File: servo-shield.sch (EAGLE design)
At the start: 23 parts, among them IC1 24AA01P, K1 PIN20X2

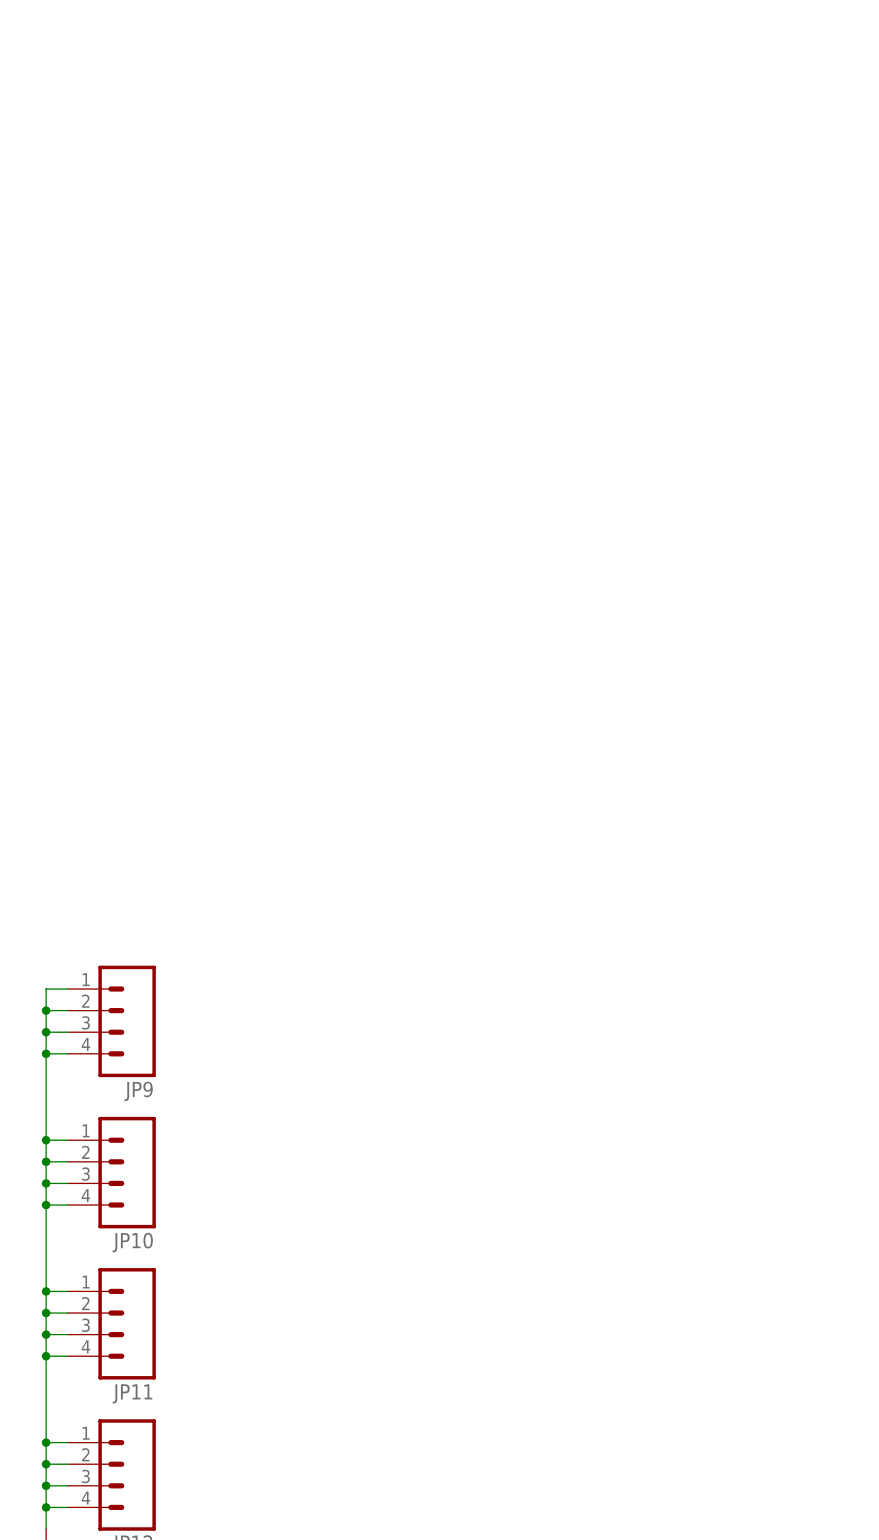
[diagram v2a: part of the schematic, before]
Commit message: Added power connector + regulator
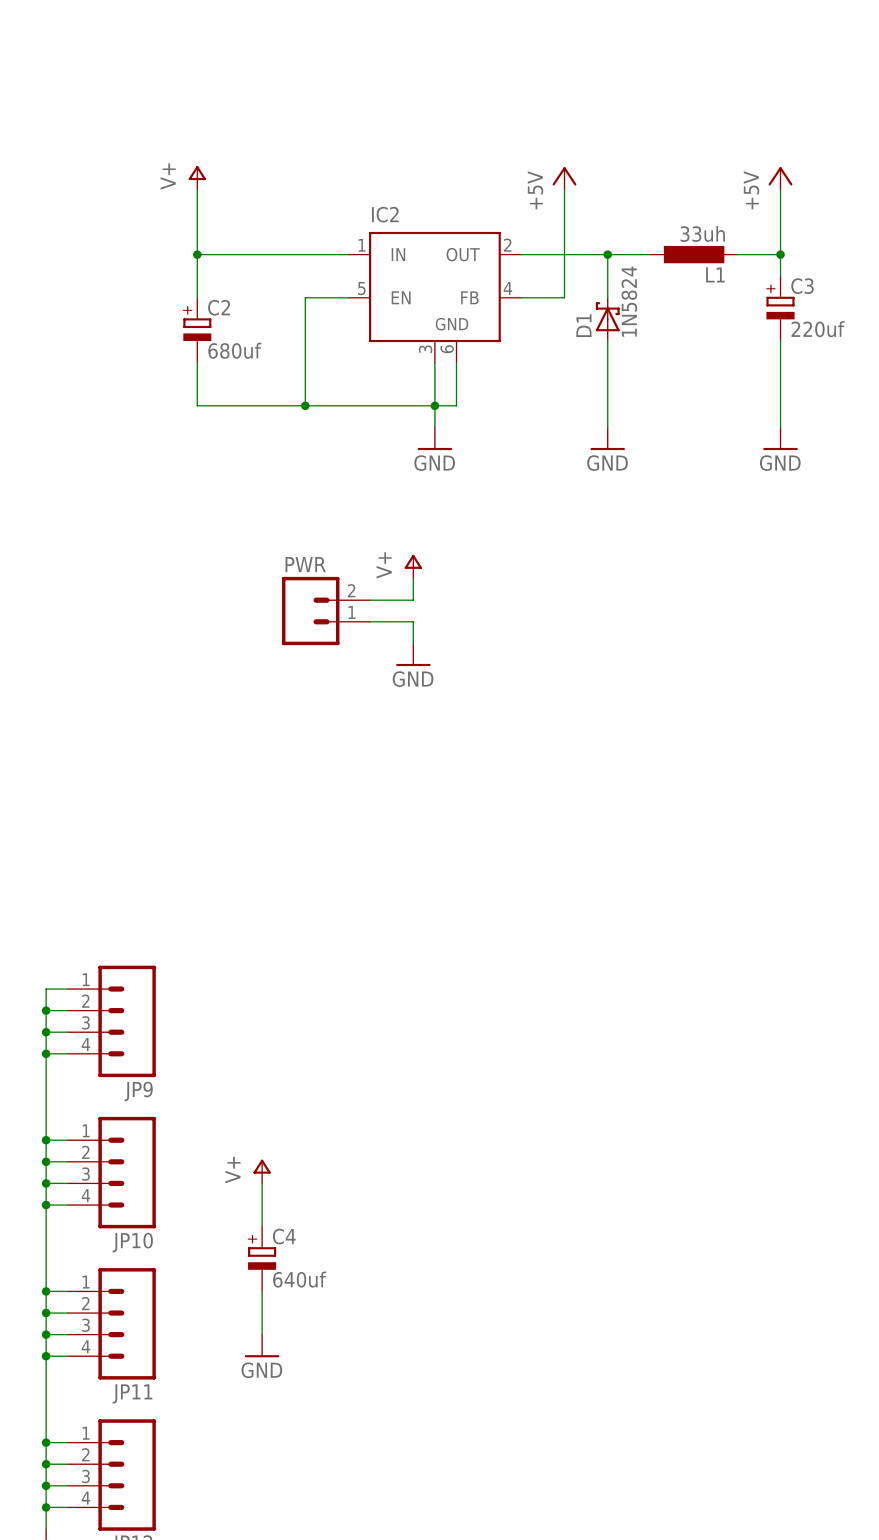
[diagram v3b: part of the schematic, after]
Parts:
- added C2: 680uf, rcl:CPOL-EUE2.5-6
- added C3: 220uf, rcl:CPOL-EUE2.5-6
- added C4: 640uf, rcl:CPOL-EUE2.5-6
- added D1: 1N5824, diode:1N5817-B
- added IC2: (no value), linear:LM2596S
- added L1: 33uh, rcl:L-EU0207/10
- added PWR: M02JST-PTH-2, SparkFun-Connectors:M02JST-PTH-2
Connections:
- new net N$40: D1.C, IC2.OUT, L1.1
- net +5V: now also C3.+, IC2.FB, L1.2
- net GND: now also C2.-, C3.-, C4.-, D1.A, IC2.EN, IC2.GND, IC2.GND@1, PWR.1
- net V+: now also C2.+, C4.+, IC2.IN, PWR.2
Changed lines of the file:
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@@
 <part name="JP11" library="SparkFun-Connectors" deviceset="M04" device="LOCK"/>
 <part name="JP12" library="SparkFun-Connectors" deviceset="M04" device="LOCK"/>
+<part name="P+2" library="supply1" deviceset="+5V" device=""/>
+<part name="P+4" library="supply1" deviceset="V+" device=""/>
+<part name="GND1" library="supply1" deviceset="GND" device=""/>
+<part name="GND6" library="supply1" deviceset="GND" device=""/>
+<part name="GND8" library="supply1" deviceset="GND" device=""/>
+<part name="GND9" library="supply1" deviceset="GND" device=""/>
+<part name="IC2" library="linear" deviceset="LM2596S" device=""/>
+<part name="C2" library="rcl" deviceset="CPOL-EU" device="E2.5-6" value="680uf"/>
+<part name="L1" library="rcl" deviceset="L-EU" device="0207/10" value="33uh"/>
+<part name="D1" library="diode" deviceset="1N581*" device="" technology="7-B" value="1N5824"/>
+<part name="P+5" library="supply1" deviceset="+5V" device=""/>
+<part name="C3" library="rcl" deviceset="CPOL-EU" device="E2.5-6" value="220uf"/>
+<part name="C4" library="rcl" deviceset="CPOL-EU" device="E2.5-6" value="640uf"/>
+<part name="P+6" library="supply1" deviceset="V+" device=""/>
+<part name="PWR" library="SparkFun-Connectors" deviceset="M02" device="JST-PTH-2" value=""/>
+<part name="P+7" library="supply1" deviceset="V+" device=""/>
+<part name="GND11" library="supply1" deviceset="GND" device=""/>
 </parts>
 <sheets>
@@
 <instance part="JP11" gate="G$1" x="208.28" y="50.8" rot="R180"/>
 <instance part="JP12" gate="G$1" x="208.28" y="33.02" rot="R180"/>
+<instance part="P+2" gate="1" x="287.02" y="185.42"/>
+<instance part="P+4" gate="1" x="218.44" y="185.42"/>
+<instance part="GND1" gate="1" x="246.38" y="152.4"/>
+<instance part="GND6" gate="1" x="266.7" y="152.4"/>
+<instance part="GND8" gate="1" x="287.02" y="152.4"/>
+<instance part="GND9" gate="1" x="226.06" y="45.72"/>
+<instance part="IC2" gate="G$1" x="246.38" y="172.72"/>
+<instance part="C2" gate="G$1" x="218.44" y="167.64"/>
+<instance part="L1" gate="G$1" x="276.86" y="175.26" rot="R90"/>
+<instance part="D1" gate="G$1" x="266.7" y="167.64" rot="R90"/>
+<instance part="P+5" gate="1" x="261.62" y="185.42"/>
+<instance part="C3" gate="G$1" x="287.02" y="170.18"/>
+<instance part="C4" gate="G$1" x="226.06" y="58.42"/>
+<instance part="P+6" gate="1" x="226.06" y="68.58"/>
+<instance part="PWR" gate="G$1" x="231.14" y="132.08"/>
+<instance part="P+7" gate="1" x="243.84" y="139.7"/>
+<instance part="GND11" gate="1" x="243.84" y="127"/>
 </instances>
 <busses>
@@
 <pinref part="JP12" gate="G$1" pin="4"/>
 </segment>
+<segment>
+<pinref part="IC2" gate="G$1" pin="EN"/>
+<wire x1="236.22" y1="170.18" x2="231.14" y2="170.18" width="0.1524" layer="91"/>
+<wire x1="231.14" y1="170.18" x2="231.14" y2="157.48" width="0.1524" layer="91"/>
+<pinref part="IC2" gate="G$1" pin="GND"/>
+<wire x1="231.14" y1="157.48" x2="246.38" y2="157.48" width="0.1524" layer="91"/>
+<wire x1="246.38" y1="162.56" x2="246.38" y2="157.48" width="0.1524" layer="91"/>
+<pinref part="GND1" gate="1" pin="GND"/>
+<wire x1="246.38" y1="154.94" x2="246.38" y2="157.48" width="0.1524" layer="91"/>
+<wire x1="246.38" y1="157.48" x2="248.92" y2="157.48" width="0.1524" layer="91"/>
+<pinref part="IC2" gate="G$1" pin="GND@1"/>
+<wire x1="248.92" y1="157.48" x2="248.92" y2="162.56" width="0.1524" layer="91"/>
+<junction x="246.38" y="157.48"/>
+<pinref part="C2" gate="G$1" pin="-"/>
+<wire x1="218.44" y1="162.56" x2="218.44" y2="157.48" width="0.1524" layer="91"/>
+<wire x1="218.44" y1="157.48" x2="231.14" y2="157.48" width="0.1524" layer="91"/>
+<junction x="231.14" y="157.48"/>
+</segment>
+<segment>
+<pinref part="GND6" gate="1" pin="GND"/>
+<pinref part="D1" gate="G$1" pin="A"/>
+<wire x1="266.7" y1="154.94" x2="266.7" y2="165.1" width="0.1524" layer="91"/>
+</segment>
+<segment>
+<pinref part="GND8" gate="1" pin="GND"/>
+<pinref part="C3" gate="G$1" pin="-"/>
+<wire x1="287.02" y1="154.94" x2="287.02" y2="165.1" width="0.1524" layer="91"/>
+</segment>
+<segment>
+<pinref part="C4" gate="G$1" pin="-"/>
+<pinref part="GND9" gate="1" pin="GND"/>
+<wire x1="226.06" y1="53.34" x2="226.06" y2="48.26" width="0.1524" layer="91"/>
+</segment>
+<segment>
+<pinref part="PWR" gate="G$1" pin="1"/>
+<wire x1="238.76" y1="132.08" x2="243.84" y2="132.08" width="0.1524" layer="91"/>
+<pinref part="GND11" gate="1" pin="GND"/>
+<wire x1="243.84" y1="132.08" x2="243.84" y2="129.54" width="0.1524" layer="91"/>
+</segment>
 </net>
 <net name="+3V3" class="0">
@@
 <wire x1="60.96" y1="172.72" x2="60.96" y2="175.26" width="0.1524" layer="91"/>
 <junction x="60.96" y="175.26"/>
+</segment>
+<segment>
+<pinref part="P+2" gate="1" pin="+5V"/>
+<wire x1="287.02" y1="175.26" x2="287.02" y2="182.88" width="0.1524" layer="91"/>
+<pinref part="L1" gate="G$1" pin="2"/>
+<wire x1="281.94" y1="175.26" x2="287.02" y2="175.26" width="0.1524" layer="91"/>
+<pinref part="C3" gate="G$1" pin="+"/>
+<wire x1="287.02" y1="172.72" x2="287.02" y2="175.26" width="0.1524" layer="91"/>
+<junction x="287.02" y="175.26"/>
+</segment>
+<segment>
+<pinref part="IC2" gate="G$1" pin="FB"/>
+<pinref part="P+5" gate="1" pin="+5V"/>
+<wire x1="256.54" y1="170.18" x2="261.62" y2="170.18" width="0.1524" layer="91"/>
+<wire x1="261.62" y1="170.18" x2="261.62" y2="182.88" width="0.1524" layer="91"/>
 </segment>
 </net>
@@
 <junction x="180.34" y="45.72"/>
 </segment>
-</net>
+<segment>
+<pinref part="P+4" gate="1" pin="V+"/>
+<wire x1="218.44" y1="182.88" x2="218.44" y2="175.26" width="0.1524" layer="91"/>
+<pinref part="IC2" gate="G$1" pin="IN"/>
+<wire x1="218.44" y1="175.26" x2="236.22" y2="175.26" width="0.1524" layer="91"/>
+<pinref part="C2" gate="G$1" pin="+"/>
+<wire x1="218.44" y1="170.18" x2="218.44" y2="175.26" width="0.1524" layer="91"/>
+<junction x="218.44" y="175.26"/>
+</segment>
+<segment>
+<pinref part="C4" gate="G$1" pin="+"/>
+<pinref part="P+6" gate="1" pin="V+"/>
+<wire x1="226.06" y1="60.96" x2="226.06" y2="66.04" width="0.1524" layer="91"/>
+</segment>
+<segment>
+<pinref part="PWR" gate="G$1" pin="2"/>
+<wire x1="238.76" y1="134.62" x2="243.84" y2="134.62" width="0.1524" layer="91"/>
+<pinref part="P+7" gate="1" pin="V+"/>
+<wire x1="243.84" y1="134.62" x2="243.84" y2="137.16" width="0.1524" layer="91"/>
+</segment>
+</net>
+<net name="N$40" class="0">
+<segment>
+<pinref part="IC2" gate="G$1" pin="OUT"/>
+<pinref part="L1" gate="G$1" pin="1"/>
+<wire x1="256.54" y1="175.26" x2="266.7" y2="175.26" width="0.1524" layer="91"/>
+<wire x1="271.78" y1="175.26" x2="266.7" y2="175.26" width="0.1524" layer="91"/>
+<wire x1="266.7" y1="175.26" x2="266.7" y2="170.18" width="0.1524" layer="91"/>
+<pinref part="D1" gate="G$1" pin="C"/>
+<junction x="266.7" y="175.26"/>
+</segment>
+</net>
